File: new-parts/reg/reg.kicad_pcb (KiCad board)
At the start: 2 copper layers, 51 parts, among them J1 BHR-10-VUA, J2 BHR-10-VUA, J3 BHR-10-VUA, J4 BHR-10-VUA, J5 Conn_01x02, J6 Conn_02x02_Odd_Even, K1 J104D2C12VDC.15S, K10 J104D2C12VDC.15S, K11 J104D2C12VDC.15S, K12 J104D2C12VDC.15S, K2 J104D2C12VDC.15S, K3 J104D2C12VDC.15S, K4 J104D2C12VDC.15S, K5 J104D2C12VDC.15S, K6 J104D2C12VDC.15S, K7 J104D2C12VDC.15S, K8 J104D2C12VDC.15S, K9 J104D2C12VDC.15S

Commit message: Finish reg.
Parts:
- D1, D2, D3, D4, D5, D6, D7, D8, R1, R2, R3, R4, R5, R6, R7, R8: moved to B.Cu
- moved R10 8.89 mm to (132.1, 52.1)
- moved R11 8.89 mm to (132.1, 80.0)
- moved R12 8.89 mm to (132.1, 77.5)
- moved R13 8.89 mm to (132.1, 105.4)
- moved R14 8.89 mm to (132.1, 102.9)
- moved R15 8.89 mm to (132.1, 130.8)
- moved R16 8.89 mm to (132.1, 128.3)
- moved R9 8.89 mm to (132.1, 54.6)
- moved R2 1.00 mm to (151.1, 61.0), turned to 90 degrees
- moved R4 1.00 mm to (151.1, 86.4), turned to 90 degrees
- moved R6 1.00 mm to (151.1, 111.8), turned to 90 degrees
- moved R8 1.00 mm to (151.1, 137.2), turned to 90 degrees
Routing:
- net VCC: track 0.00 -> 415.2 mm, vias 0 -> 8
- net Net-(D9-A1): track 42.2 -> 129.2 mm, vias 0 -> 6
- net Net-(J1-Pin_8): track 0.00 -> 79.8 mm, vias 0 -> 2
- net Net-(J2-Pin_1): track 0.00 -> 75.3 mm, vias 0 -> 1
- net Net-(J2-Pin_2): track 0.00 -> 69.7 mm, vias 0 -> 1
- net Net-(J1-Pin_7): track 0.00 -> 63.8 mm, vias 0 -> 2
- net Net-(J2-Pin_8): track 0.00 -> 58.7 mm, vias 0 -> 2
- net Net-(J1-Pin_6): track 0.00 -> 57.3 mm, vias 0 -> 2
- net Net-(J1-Pin_1): track 0.00 -> 55.4 mm, vias 0 -> 1
- net Net-(J2-Pin_3): track 0.00 -> 52.1 mm, vias 0 -> 1
- net Net-(J2-Pin_4): track 0.00 -> 48.1 mm, vias 0 -> 1
- net Net-(J2-Pin_7): track 0.00 -> 45.0 mm, vias 0 -> 2
- net Net-(J1-Pin_2): track 0.00 -> 42.4 mm, vias 0 -> 1
- net Net-(J1-Pin_3): track 0.00 -> 40.9 mm, vias 0 -> 2
- net Net-(J1-Pin_5): track 0.00 -> 40.2 mm, vias 0 -> 2
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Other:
- board outline added: 104.1 x 113 mm
- board text added: "Clock"
- board text added: "In"
- board text added: "Out"
- board text added: "Override"
- board text added: "Power"
- board text added: "~{Out}"
- board text removed: "Test"

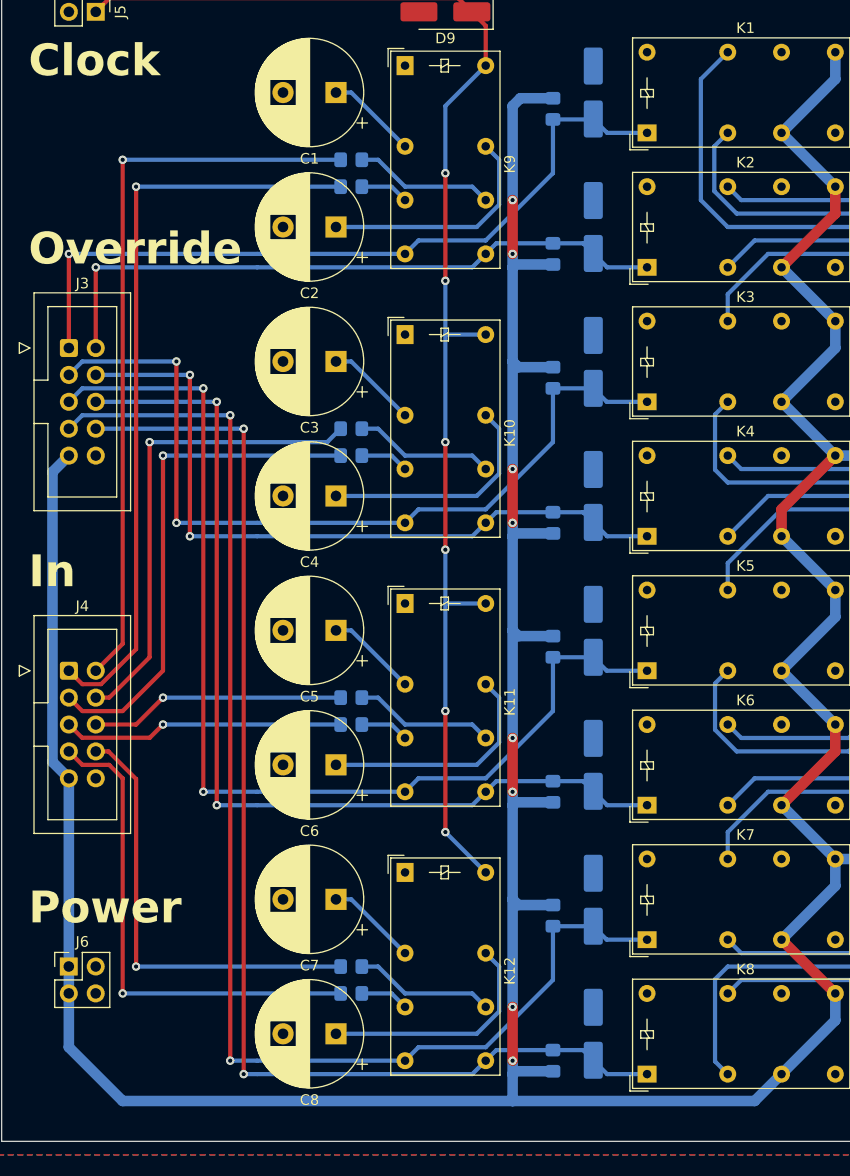
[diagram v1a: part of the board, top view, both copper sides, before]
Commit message: Reverse clock polarity.
It's more convenient to have the registers sample the input while the
clock is high, and latch it to the output on the falling edge. That way,
a register whose clock input is kept low or Z will not change (otherwise,
we would have to keep idle registers' clock inputs high).
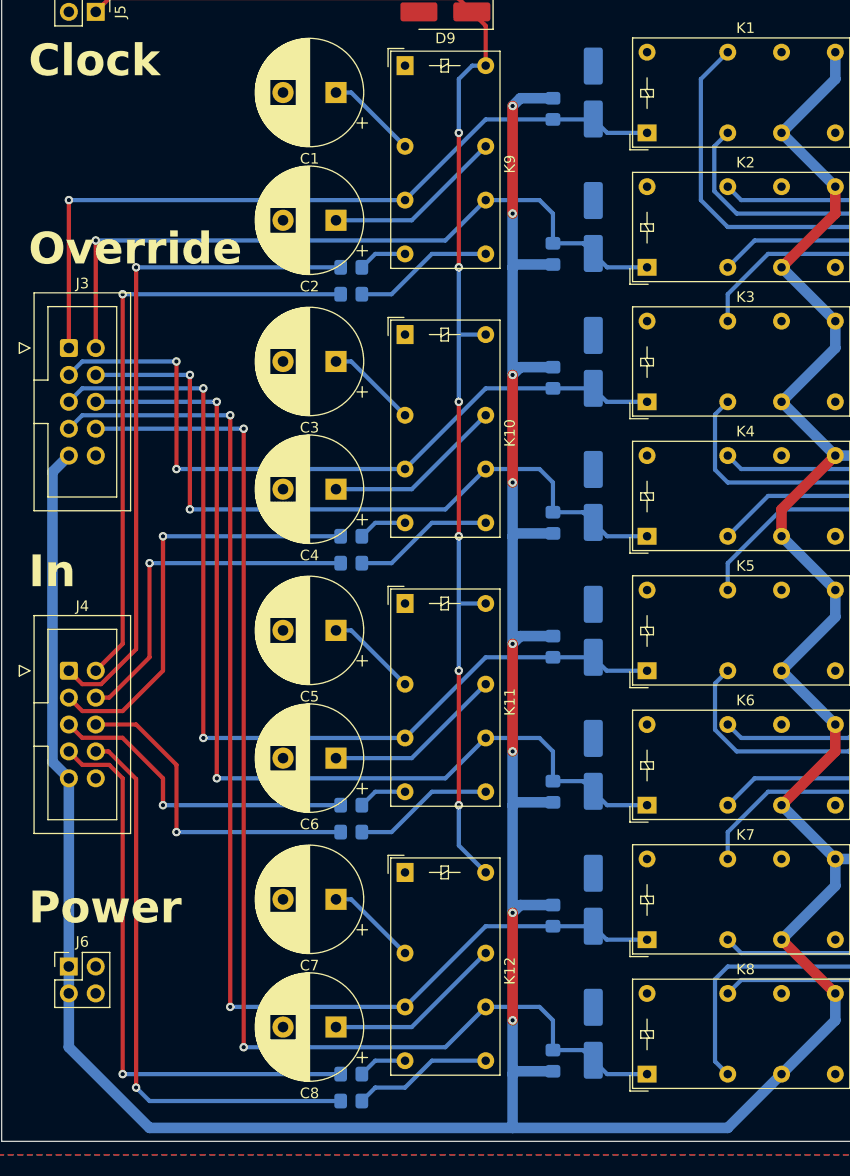
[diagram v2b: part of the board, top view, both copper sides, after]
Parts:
- moved R12 12.7 mm to (132.1, 90.2)
- moved R10 12.7 mm to (132.1, 64.8)
- moved R14 12.7 mm to (132.1, 115.6)
- moved R16 12.7 mm to (132.1, 141.0)
- moved R13 7.62 mm to (132.1, 113.0)
- moved R15 7.62 mm to (132.1, 138.4)
- moved R9 7.62 mm to (132.1, 62.2)
- moved R11 7.62 mm to (132.1, 87.6)
- moved C2 0.64 mm to (130.6, 57.8)
- moved C6 0.64 mm to (130.6, 108.6)
- moved C4 0.63 mm to (130.6, 83.2)
- moved C8 0.63 mm to (130.6, 134.0)
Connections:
- K10 pad 12: Net-(K10-Pad12) -> Net-(D3-A2)
- K10 pad 14: Net-(D3-A2) -> Net-(K10-Pad14)
- K10 pad 22: Net-(K10-Pad22) -> Net-(D4-A2)
- K10 pad 24: Net-(D4-A2) -> Net-(K10-Pad24)
- K11 pad 12: Net-(K11-Pad12) -> Net-(D5-A2)
- K11 pad 14: Net-(D5-A2) -> Net-(K11-Pad14)
- K11 pad 22: Net-(K11-Pad22) -> Net-(D6-A2)
- K11 pad 24: Net-(D6-A2) -> Net-(K11-Pad24)
- K12 pad 12: Net-(K12-Pad12) -> Net-(D7-A2)
- K12 pad 14: Net-(D7-A2) -> Net-(K12-Pad14)
- K12 pad 22: Net-(K12-Pad22) -> Net-(D8-A2)
- K12 pad 24: Net-(D8-A2) -> Net-(K12-Pad24)
- K9 pad 12: Net-(K9-Pad12) -> Net-(D1-A2)
- K9 pad 14: Net-(D1-A2) -> Net-(K9-Pad14)
- K9 pad 22: Net-(K9-Pad22) -> Net-(D2-A2)
- K9 pad 24: Net-(D2-A2) -> Net-(K9-Pad24)
- R10 pad 1: Net-(K9-Pad22) -> Net-(K9-Pad24)
- R11 pad 1: Net-(K10-Pad12) -> Net-(K10-Pad14)
- R12 pad 1: Net-(K10-Pad22) -> Net-(K10-Pad24)
- R13 pad 1: Net-(K11-Pad12) -> Net-(K11-Pad14)
- R14 pad 1: Net-(K11-Pad22) -> Net-(K11-Pad24)
- R15 pad 1: Net-(K12-Pad12) -> Net-(K12-Pad14)
- R16 pad 1: Net-(K12-Pad22) -> Net-(K12-Pad24)
- R9 pad 1: Net-(K9-Pad12) -> Net-(K9-Pad14)
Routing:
- net Net-(K10-Pad24): track 0.00 -> 13.4 mm
- net Net-(K12-Pad24): track 0.00 -> 13.3 mm
- net Net-(K9-Pad22): track 13.3 -> 0.00 mm
- net Net-(K11-Pad22): track 13.3 -> 0.00 mm
- net Net-(K10-Pad22): track 13.3 -> 0.00 mm
- net Net-(K12-Pad22): track 13.3 -> 0.00 mm
- net Net-(K9-Pad24): track 0.00 -> 13.3 mm
- net Net-(K11-Pad24): track 0.00 -> 13.3 mm
- net Net-(J4-Pin_2): track 69.9 -> 57.2 mm
- net Net-(J4-Pin_4): track 45.6 -> 33.6 mm
- net Net-(J4-Pin_8): track 41.9 -> 53.9 mm
- net Net-(D5-A2): track 102.0 -> 91.8 mm
- net Net-(D3-A2): track 79.1 -> 69.0 mm
- net Net-(D7-A2): track 124.9 -> 114.7 mm
- net Net-(J4-Pin_7): track 47.0 -> 54.7 mm
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
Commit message: reg: Clarify labels.
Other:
- board text added: "+ -"
- board text added: "GND Clock"
- board text removed: "Clock"
- board text removed: "Power"
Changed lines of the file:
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@@
     (property "ki_keywords" "connector")
     (attr through_hole)
-    (fp_text reference "J6" (at 1.27 -2.33) (layer "F.SilkS")
+    (fp_text reference "J6" (at -2.535 1.275 90) (layer "F.SilkS")
         (effects (font (size 1 1) (thickness 0.15)))
     )
@@
   (gr_line (start 203.2 144.78) (end 203.2 31.75)
     (stroke (width 0.1) (type default)) (layer "Edge.Cuts"))
-  (gr_text "Power" (at 101.6 124.46) (layer "F.SilkS")
-    (effects (font (size 3 3) (thickness 0.6) bold) (justify left bottom))
+  (gr_text "+\n-" (at 106.68 123.19 90) (layer "F.SilkS")
+    (effects (font (size 3 3) (thickness 0.6) bold))
   )
   (gr_text "Out" (at 189.23 62.23) (layer "F.SilkS")
@@
     (effects (font (size 3 3) (thickness 0.6) bold) (justify left bottom))
   )
+  (gr_text "+\n-" (at 106.68 135.89 90) (layer "F.SilkS")
+    (effects (font (size 3 3) (thickness 0.6) bold))
+  )
   (gr_text "In" (at 101.6 92.71) (layer "F.SilkS")
     (effects (font (size 3 3) (thickness 0.6) bold) (justify left bottom))
@@
     (effects (font (size 3 3) (thickness 0.6) bold) (justify left bottom))
   )
-  (gr_text "Clock" (at 101.6 44.45) (layer "F.SilkS")
-    (effects (font (size 3 3) (thickness 0.6) bold) (justify left bottom))
+  (gr_text "GND\nClock" (at 106.68 40.64 90) (layer "F.SilkS")
+    (effects (font (size 3 3) (thickness 0.6) bold) (justify right))
   )
   (dimension (type aligned) (layer "Dwgs.User")

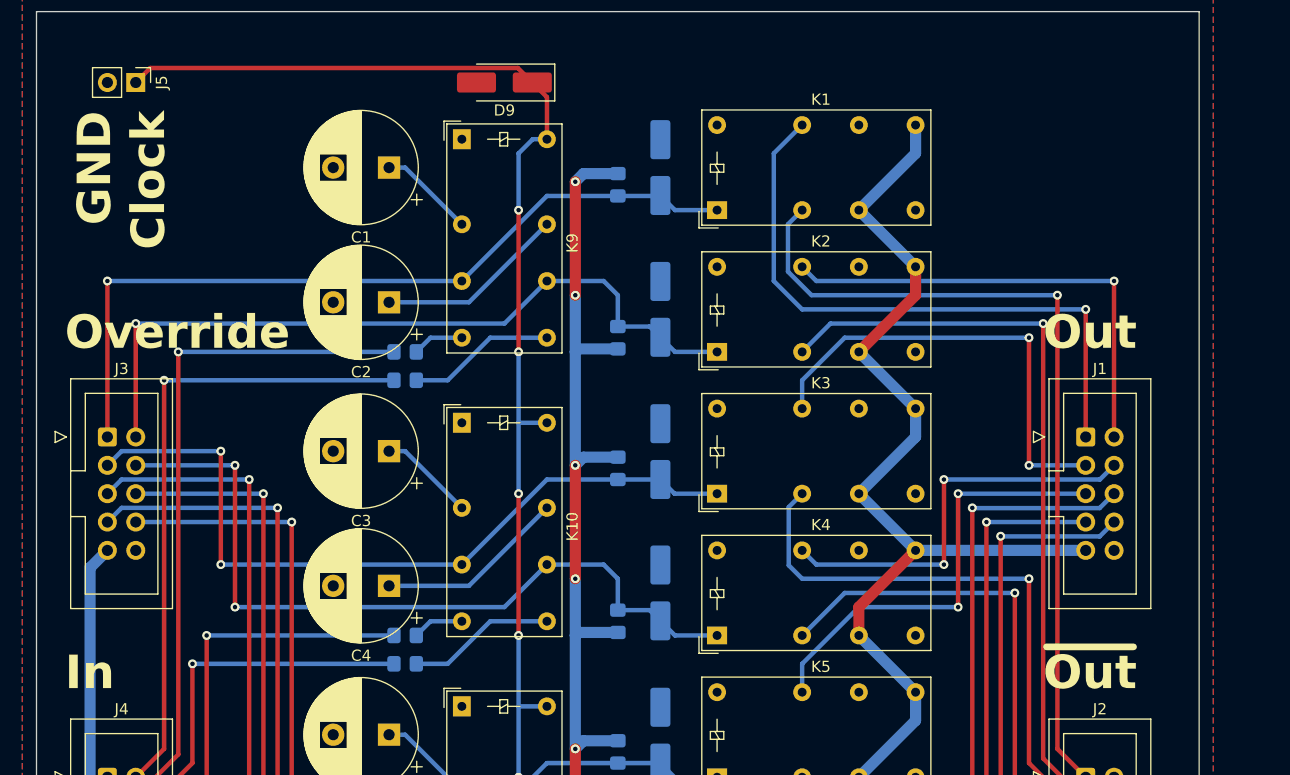
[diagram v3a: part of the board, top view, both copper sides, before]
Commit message: Change all two-pin headers for control + ground to control only.
This is to prevent accidental short circuits when they are plugged in the
wrong way.
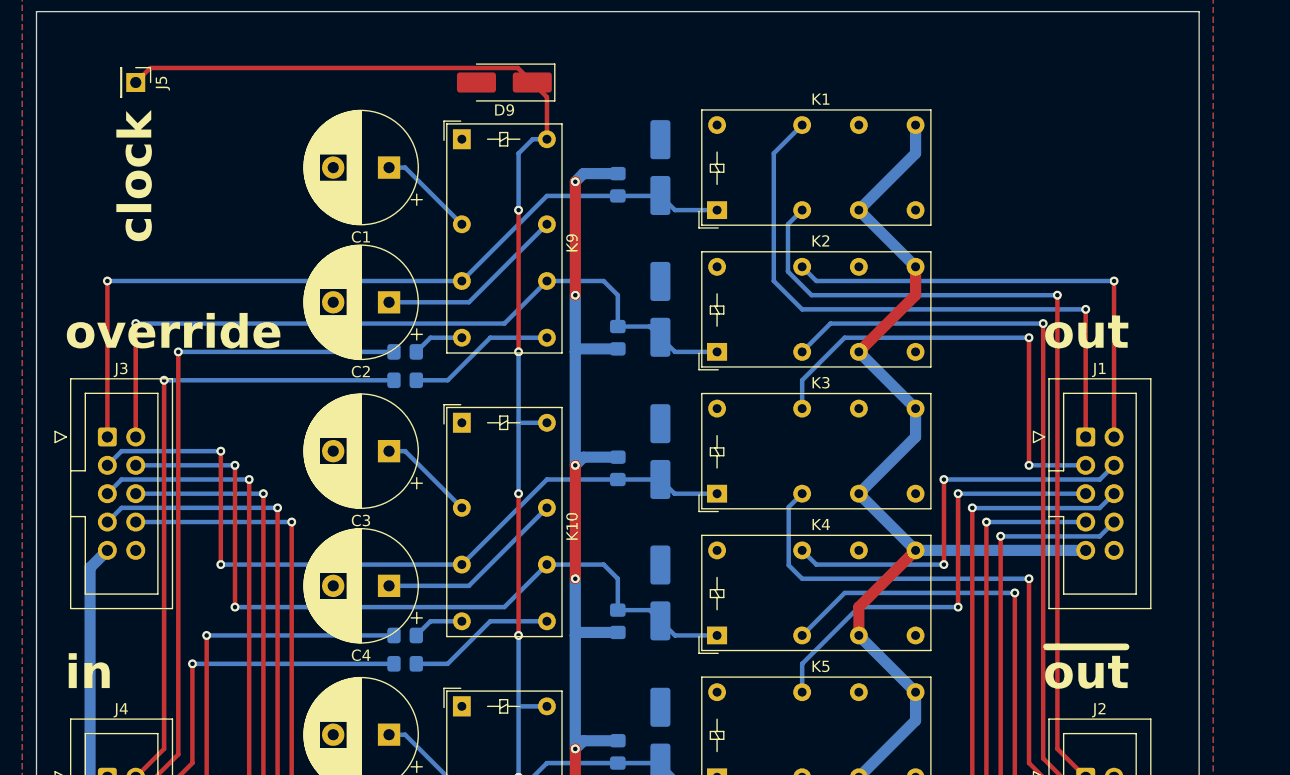
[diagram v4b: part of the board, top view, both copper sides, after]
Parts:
- J5: footprint Connector_PinHeader_2.54mm:PinHeader_1x02_P2.54mm_Vertical -> Connector_PinHeader_2.54mm:PinHeader_1x01_P2.54mm_Vertical
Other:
- board text added: "clock"
- board text added: "in"
- board text added: "out"
- board text added: "override"
- board text added: "~{out}"
- board text removed: "GND Clock"
- board text removed: "In"
- board text removed: "Out"
- board text removed: "Override"
- board text removed: "~{Out}"
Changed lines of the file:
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@@
     )
   )
-  (footprint "Connector_PinHeader_2.54mm:PinHeader_1x02_P2.54mm_Vertical" (layer "F.Cu")
+  (footprint "Connector_PinHeader_2.54mm:PinHeader_1x01_P2.54mm_Vertical" (layer "F.Cu")
     (at 107.95 38.1 -90)
-    (descr "Through hole straight pin header, 1x02, 2.54mm pitch, single row")
-    (tags "Through hole pin header THT 1x02 2.54mm single row")
-    (property "Sheetfile" "reg.kicad_sch")
-    (property "Sheetname" "")
-    (property "ki_description" "Generic connector, single row, 01x02, script generated (kicad-library-utils/schlib/autogen/connector/)")
+    (descr "Through hole straight pin header, 1x01, 2.54mm pitch, single row")
+    (tags "Through hole pin header THT 1x01 2.54mm single row")
+    (property "Sheetfile" "reg.kicad_sch")
+    (property "Sheetname" "")
+    (property "ki_description" "Generic connector, single row, 01x01, script generated (kicad-library-utils/schlib/autogen/connector/)")
     (property "ki_keywords" "connector")
     (attr through_hole)
-    (fp_text reference "J5" (at 0 -2.33 90) (layer "F.SilkS")
+    (fp_text reference "J5" (at 0 -2.33 -90) (layer "F.SilkS")
         (effects (font (size 1 1) (thickness 0.15)))
     )
-    (fp_text value "Conn_01x02" (at 0 4.87 90) (layer "F.Fab")
+    (fp_text value "Conn_01x02" (at 0 2.33 -90) (layer "F.Fab")
         (effects (font (size 1 1) (thickness 0.15)))
     )
-    (fp_text user "${REFERENCE}" (at 0 1.27) (layer "F.Fab")
+    (fp_text user "${REFERENCE}" (at 0 0) (layer "F.Fab")
         (effects (font (size 1 1) (thickness 0.15)))
     )
@@
     (fp_line (start -1.33 0) (end -1.33 -1.33)
       (stroke (width 0.12) (type solid)) (layer "F.SilkS"))
-    (fp_line (start -1.33 1.27) (end -1.33 3.87)
+    (fp_line (start -1.33 1.27) (end -1.33 1.33)
       (stroke (width 0.12) (type solid)) (layer "F.SilkS"))
     (fp_line (start -1.33 1.27) (end 1.33 1.27)
       (stroke (width 0.12) (type solid)) (layer "F.SilkS"))
-    (fp_line (start -1.33 3.87) (end 1.33 3.87)
+    (fp_line (start -1.33 1.33) (end 1.33 1.33)
       (stroke (width 0.12) (type solid)) (layer "F.SilkS"))
-    (fp_line (start 1.33 1.27) (end 1.33 3.87)
+    (fp_line (start 1.33 1.27) (end 1.33 1.33)
       (stroke (width 0.12) (type solid)) (layer "F.SilkS"))
-    (fp_line (start -1.8 -1.8) (end -1.8 4.35)
+    (fp_line (start -1.8 -1.8) (end -1.8 1.8)
       (stroke (width 0.05) (type solid)) (layer "F.CrtYd"))
-    (fp_line (start -1.8 4.35) (end 1.8 4.35)
+    (fp_line (start -1.8 1.8) (end 1.8 1.8)
       (stroke (width 0.05) (type solid)) (layer "F.CrtYd"))
     (fp_line (start 1.8 -1.8) (end -1.8 -1.8)
       (stroke (width 0.05) (type solid)) (layer "F.CrtYd"))
-    (fp_line (start 1.8 4.35) (end 1.8 -1.8)
+    (fp_line (start 1.8 1.8) (end 1.8 -1.8)
       (stroke (width 0.05) (type solid)) (layer "F.CrtYd"))
     (fp_line (start -1.27 -0.635) (end -0.635 -1.27)
       (stroke (width 0.1) (type solid)) (layer "F.Fab"))
-    (fp_line (start -1.27 3.81) (end -1.27 -0.635)
+    (fp_line (start -1.27 1.27) (end -1.27 -0.635)
       (stroke (width 0.1) (type solid)) (layer "F.Fab"))
     (fp_line (start -0.635 -1.27) (end 1.27 -1.27)
       (stroke (width 0.1) (type solid)) (layer "F.Fab"))
-    (fp_line (start 1.27 -1.27) (end 1.27 3.81)
+    (fp_line (start 1.27 -1.27) (end 1.27 1.27)
       (stroke (width 0.1) (type solid)) (layer "F.Fab"))
-    (fp_line (start 1.27 3.81) (end -1.27 3.81)
+    (fp_line (start 1.27 1.27) (end -1.27 1.27)
       (stroke (width 0.1) (type solid)) (layer "F.Fab"))
     (pad "1" thru_hole rect (at 0 0 270) (size 1.7 1.7) (drill 1) (layers "*.Cu" "*.Mask")
       (net 18 "Net-(D9-A1)") (pinfunction "Pin_1") (pintype "passive"))
-    (pad "2" thru_hole oval (at 0 2.54 270) (size 1.7 1.7) (drill 1) (layers "*.Cu" "*.Mask")
-      (net 16 "GND") (pinfunction "Pin_2") (pintype "passive"))
-    (model "${KICAD6_3DMODEL_DIR}/Connector_PinHeader_2.54mm.3dshapes/PinHeader_1x02_P2.54mm_Vertical.wrl"
+    (model "${KICAD6_3DMODEL_DIR}/Connector_PinHeader_2.54mm.3dshapes/PinHeader_1x01_P2.54mm_Vertical.wrl"
       (offset (xyz 0 0 0))
       (scale (xyz 1 1 1))
@@
     (effects (font (size 3 3) (thickness 0.6) bold))
   )
-  (gr_text "Out" (at 189.23 62.23) (layer "F.SilkS")
+  (gr_text "out" (at 189.23 62.23) (layer "F.SilkS")
     (effects (font (size 3 3) (thickness 0.6) bold) (justify left bottom))
   )
-  (gr_text "~{Out}" (at 189.23 92.71) (layer "F.SilkS")
+  (gr_text "~{out}" (at 189.23 92.71) (layer "F.SilkS")
     (effects (font (size 3 3) (thickness 0.6) bold) (justify left bottom))
   )
@@
     (effects (font (size 3 3) (thickness 0.6) bold))
   )
-  (gr_text "In" (at 101.6 92.71) (layer "F.SilkS")
+  (gr_text "in" (at 101.6 92.71) (layer "F.SilkS")
     (effects (font (size 3 3) (thickness 0.6) bold) (justify left bottom))
   )
-  (gr_text "Override" (at 101.6 62.23) (layer "F.SilkS")
+  (gr_text "override" (at 101.6 62.23) (layer "F.SilkS")
     (effects (font (size 3 3) (thickness 0.6) bold) (justify left bottom))
   )
-  (gr_text "GND\nClock" (at 106.68 40.64 90) (layer "F.SilkS")
+  (gr_text "clock" (at 107.95 40.64 90) (layer "F.SilkS")
     (effects (font (size 3 3) (thickness 0.6) bold) (justify right))
   )

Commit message: Add placeholders for JLC order number.
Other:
- board text added: "JLCJLCJLCJLC"
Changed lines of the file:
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@@
   (gr_line (start 203.2 144.78) (end 203.2 31.75)
     (stroke (width 0.1) (type default)) (layer "Edge.Cuts"))
+  (gr_text "JLCJLCJLCJLC" (at 201.676 143.256) (layer "B.SilkS")
+    (effects (font (size 1 1) (thickness 0.15)) (justify left bottom mirror))
+  )
   (gr_text "+\n-" (at 106.68 123.19 90) (layer "F.SilkS")
     (effects (font (size 3 3) (thickness 0.6) bold))

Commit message: Add a "title" label to all parts.
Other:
- board text added: "vis vitalis register"
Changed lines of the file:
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@@
     (effects (font (size 1 1) (thickness 0.15)) (justify left bottom mirror))
+  )
+  (gr_text "vis vitalis\nregister" (at 194.31 139.7 270) (layer "B.SilkS")
+    (effects (font (size 3 3) (thickness 0.6) bold) (justify left mirror))
   )
   (gr_text "+\n-" (at 106.68 123.19 90) (layer "F.SilkS")
